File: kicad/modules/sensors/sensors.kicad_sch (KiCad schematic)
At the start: 34 parts, among them J1 Bus_PCI_Express_x1, J2 TYPE-C-31-M-04, J4 Conn_01x02, U2 RP2040, U4 W25Q128JVP, U9 MCP25625T-E/ML, X1 ABM8-272-T3, Y2 X322516MLB4SI

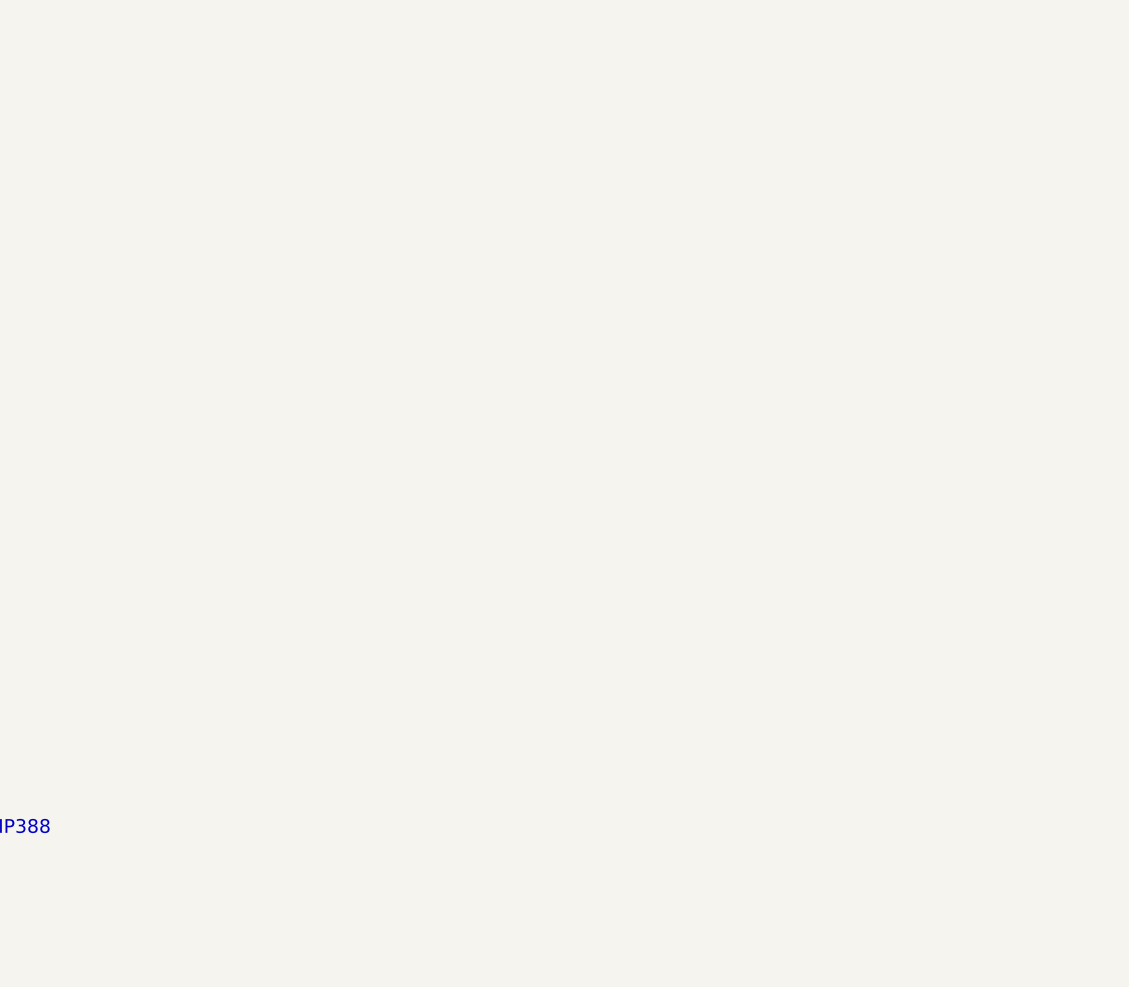
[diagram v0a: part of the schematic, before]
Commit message: add new sensors, LDO and MOSFET
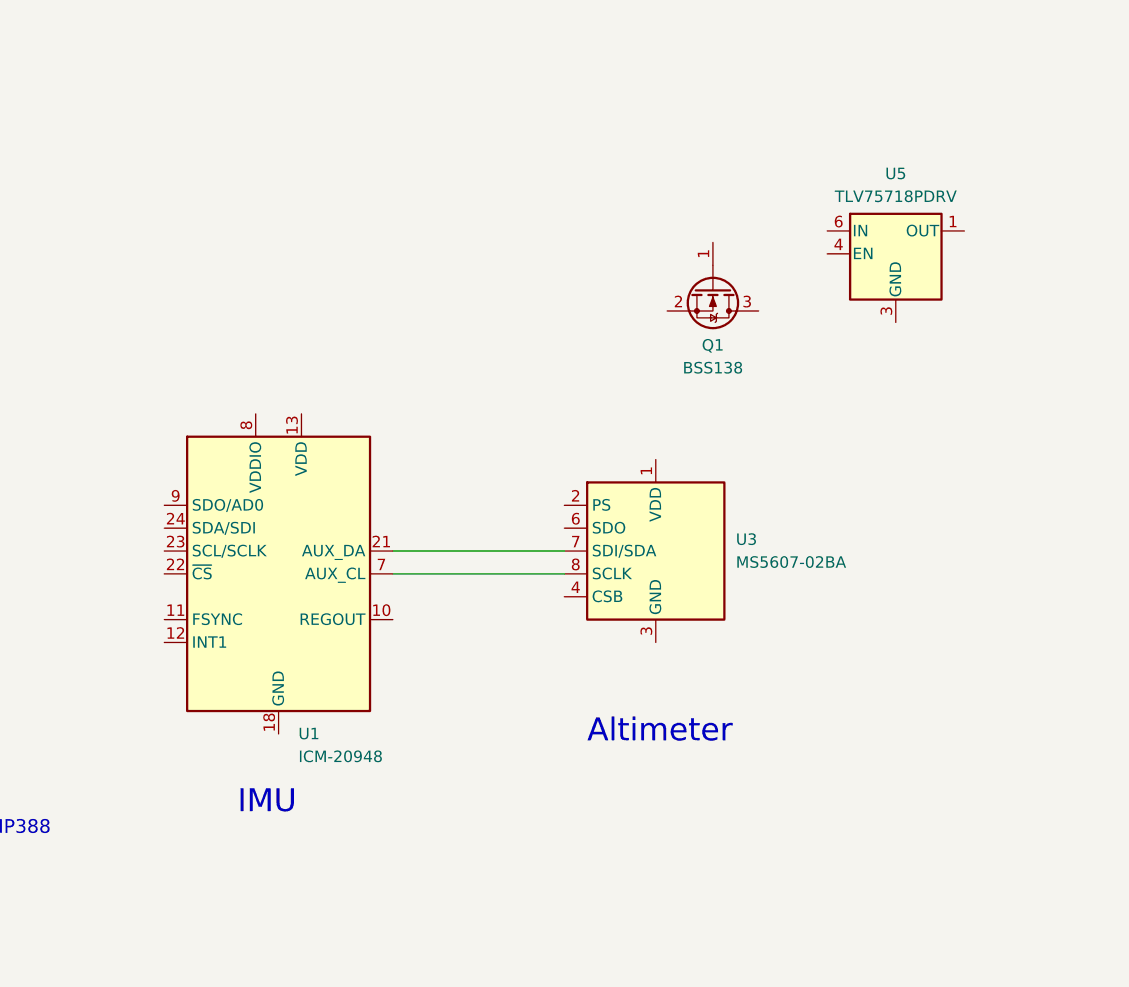
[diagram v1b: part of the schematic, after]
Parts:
- added Q1: BSS138, Package_TO_SOT_SMD:SOT-23, symbol Transistor_FET:BSS138
- added U1: ICM-20948, Sensor_Motion:InvenSense_QFN-24_3x3mm_P0.4mm, symbol Sensor_Motion:ICM-20948
- added U3: MS5607-02BA, Package_LGA:LGA-8_3x5mm_P1.25mm, symbol Sensor_Pressure:MS5607-02BA
- added U5: TLV75718PDRV, Package_SON:WSON-6-1EP_2x2mm_P0.65mm_EP1x1.6mm, symbol Regulator_Linear:TLV75718PDRV
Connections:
- new net: U3.4 (CSB), U3.5 (CSB)
- new net: U1.21 (AUX_DA), U3.7 (SDI/SDA)
- new net: U1.7 (AUX_CL), U3.8 (SCLK)
- new net: U5.3 (GND), U5.7 (GND)
- new net: U1.18 (GND), U1.20 (GND)
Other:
- note added: "Altimeter"
- note added: "IMU"
